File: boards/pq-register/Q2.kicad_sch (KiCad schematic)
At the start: 94 parts, among them Q100 MMBT5401, Q65 MMBT5401, Q73 MMBT5401, Q74 MMBT5401, Q75 MMBT5401, Q76 MMBT5401, Q77 MMBT5401, Q78 MMBT5401, Q79 MMBT5401, Q80 MMBT5401, Q81 MMBT5401, Q82 MMBT5401

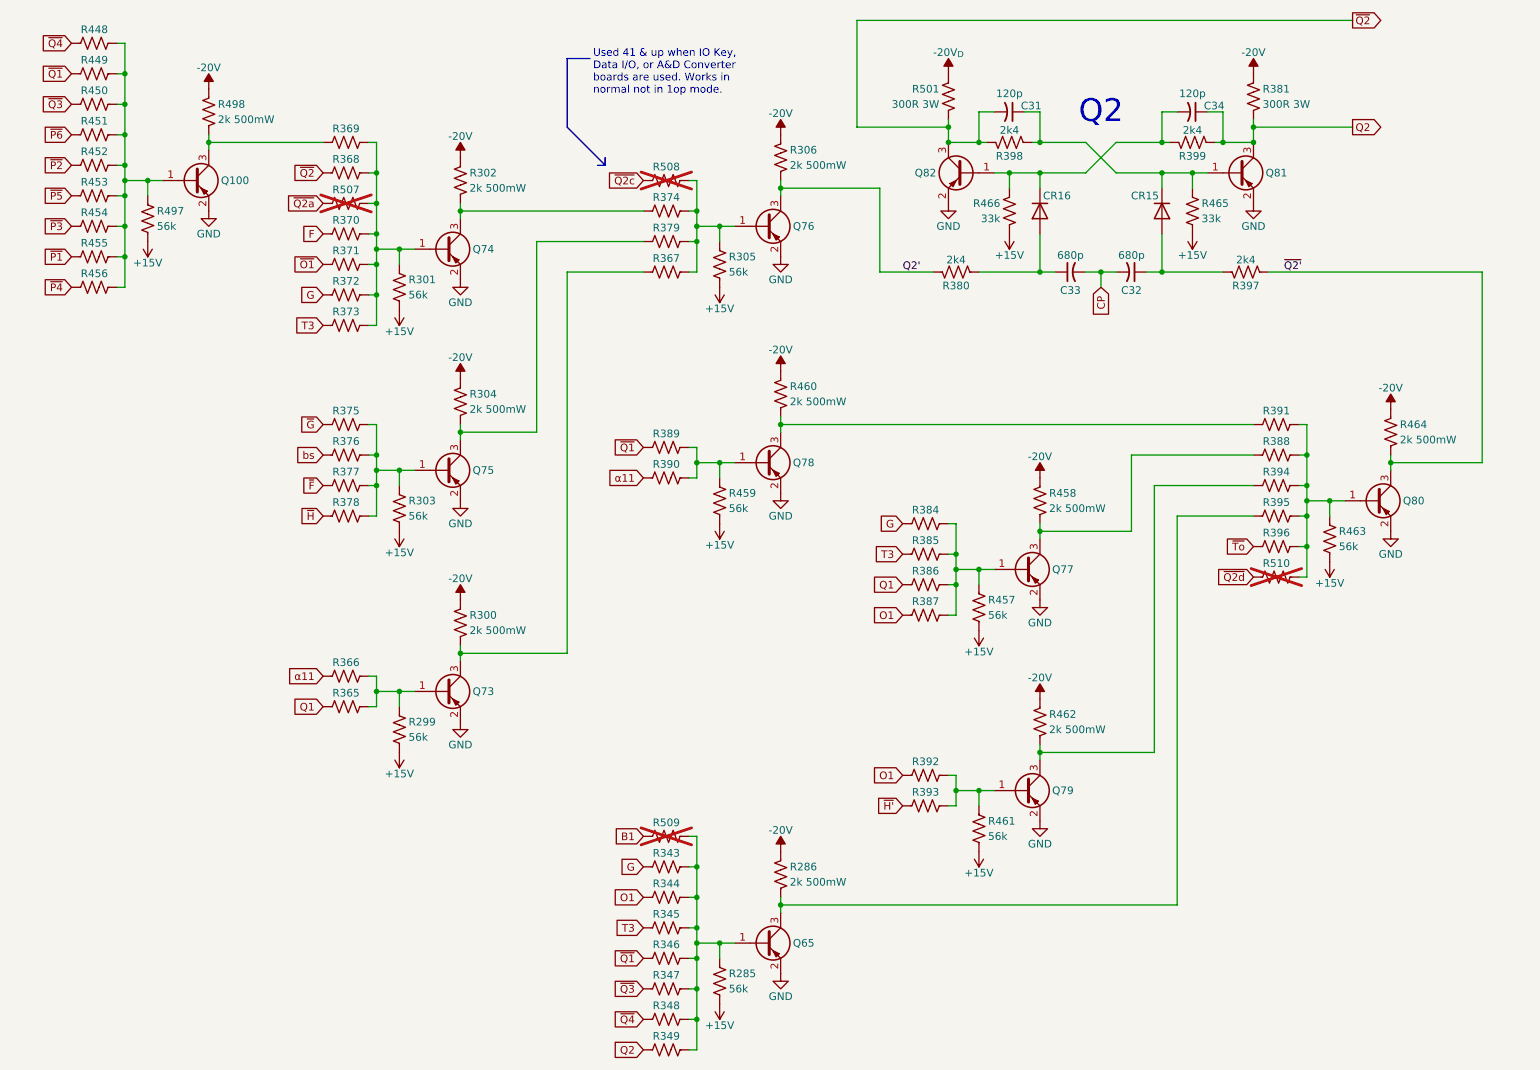
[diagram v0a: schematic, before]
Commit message: Better PCI footprint, more layout.
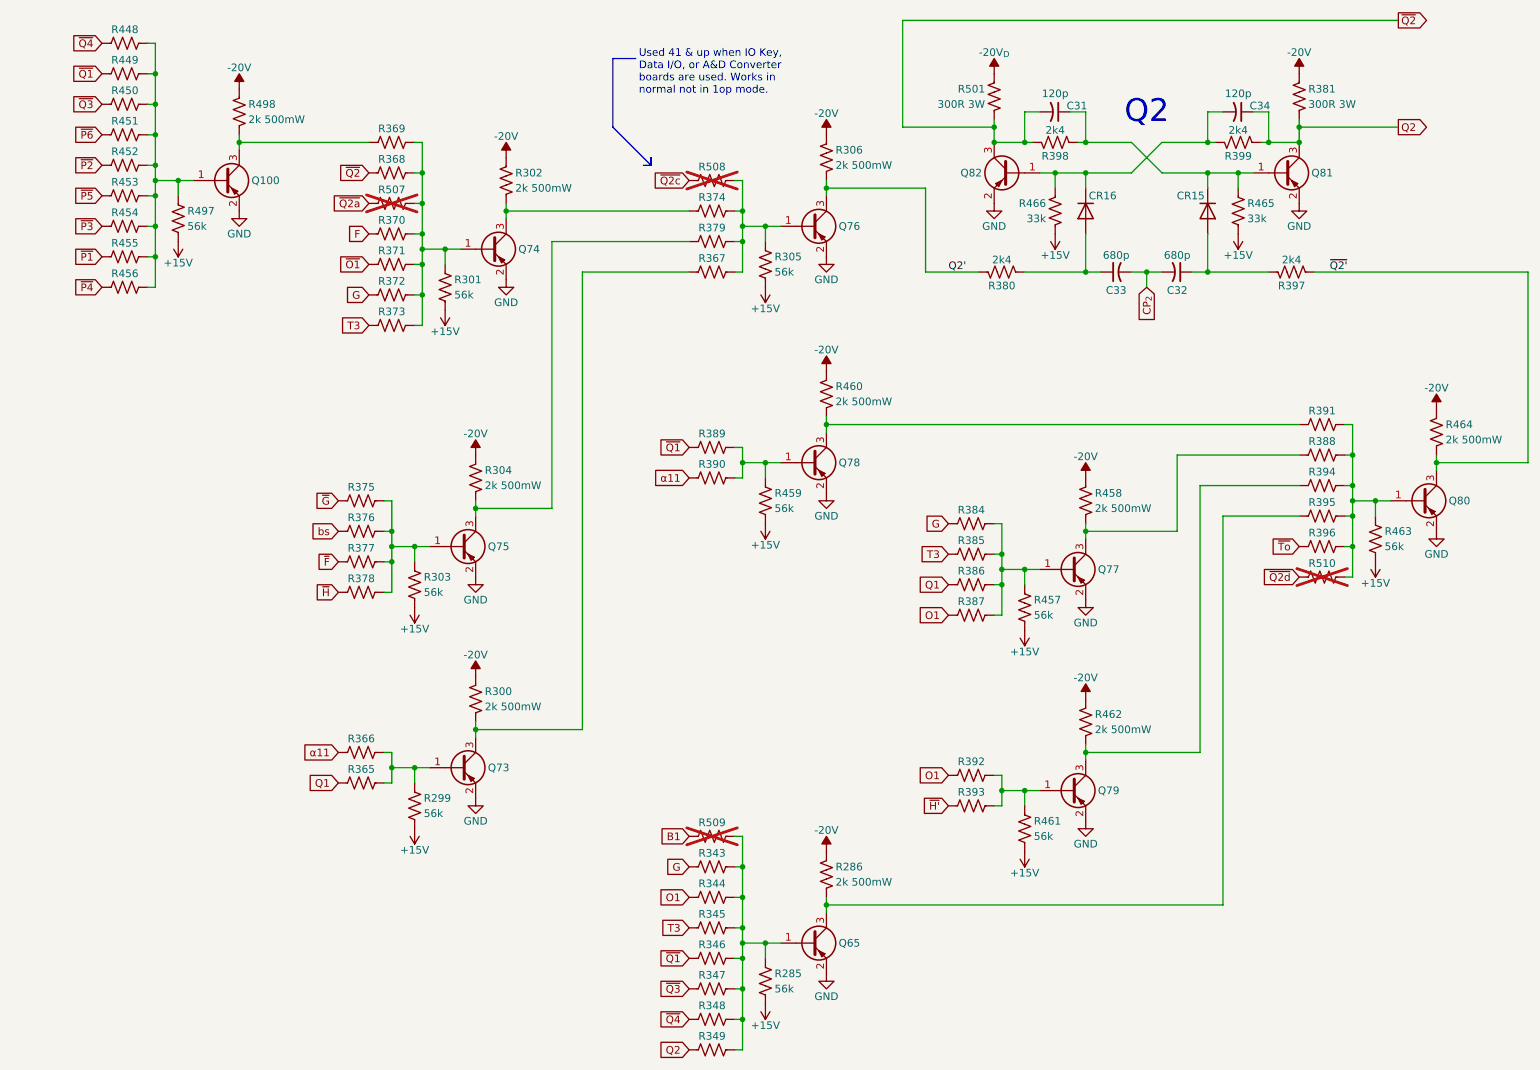
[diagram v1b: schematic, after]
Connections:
- net CP renamed CP_{2}
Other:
- moved on the sheet: C31, C32, C33, C34, CR15, CR16, Q100, Q65, Q73, Q74, Q75, Q76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

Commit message: Start updating 2k4 resistors to 0603, melt some traces.
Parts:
- R286, R300, R302, R304, R306, R458, R460, R462, R464, R498: value 2k 500mW -> 2k ½W
- R380, R397, R398, R399: value 2k4 -> 2k4 ¼W; footprint Resistor_SMD:R_0402_1005Metric -> Resistor_SMD:R_0603_1608Metric
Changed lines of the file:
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@@
 			)
 		)
-		(property "Value" "2k 500mW"
+		(property "Value" "2k ½W"
 			(at 90.424 135.89 0)
 			(show_name no)
@@
 			)
 		)
-		(property "Value" "2k 500mW"
+		(property "Value" "2k ½W"
 			(at 90.424 99.06 0)
 			(show_name no)
@@
 			)
 		)
-		(property "Value" "2k 500mW"
+		(property "Value" "2k ½W"
 			(at 250.444 91.44 0)
 			(show_name no)
@@
 			)
 		)
-		(property "Value" "2k4"
+		(property "Value" "2k4 ¼W"
 			(at 215.9 39.878 90)
 			(show_name no)
@@
 			)
 		)
-		(property "Footprint" "Resistor_SMD:R_0402_1005Metric"
+		(property "Footprint" "Resistor_SMD:R_0603_1608Metric"
 			(at 216.154 42.926 90)
 			(hide yes)
@@
 			)
 		)
-		(property "Value" "2k 500mW"
+		(property "Value" "2k ½W"
 			(at 192.024 102.87 0)
 			(show_name no)
@@
 			)
 		)
-		(property "Value" "2k 500mW"
+		(property "Value" "2k ½W"
 			(at 51.054 38.1 0)
 			(show_name no)
@@
 			)
 		)
-		(property "Value" "2k4"
+		(property "Value" "2k4 ¼W"
 			(at 176.53 61.468 90)
 			(show_name no)
@@
 			)
 		)
-		(property "Footprint" "Resistor_SMD:R_0402_1005Metric"
+		(property "Footprint" "Resistor_SMD:R_0603_1608Metric"
 			(at 176.784 64.516 90)
 			(hide yes)
@@
 			)
 		)
-		(property "Value" "2k 500mW"
+		(property "Value" "2k ½W"
 			(at 148.844 45.72 0)
 			(show_name no)
@@
 			)
 		)
-		(property "Value" "2k 500mW"
+		(property "Value" "2k ½W"
 			(at 95.504 49.53 0)
 			(show_name no)
@@
 			)
 		)
-		(property "Value" "2k4"
+		(property "Value" "2k4 ¼W"
 			(at 185.42 39.878 90)
 			(show_name no)
@@
 			)
 		)
-		(property "Footprint" "Resistor_SMD:R_0402_1005Metric"
+		(property "Footprint" "Resistor_SMD:R_0603_1608Metric"
 			(at 185.674 42.926 90)
 			(hide yes)
@@
 			)
 		)
-		(property "Value" "2k 500mW"
+		(property "Value" "2k ½W"
 			(at 148.844 85.09 0)
 			(show_name no)
@@
 			)
 		)
-		(property "Value" "2k 500mW"
+		(property "Value" "2k ½W"
 			(at 192.024 139.7 0)
 			(show_name no)
@@
 			)
 		)
-		(property "Value" "2k 500mW"
+		(property "Value" "2k ½W"
 			(at 148.844 165.1 0)
 			(show_name no)
@@
 			)
 		)
-		(property "Value" "2k4"
+		(property "Value" "2k4 ¼W"
 			(at 224.79 61.468 90)
 			(show_name no)
@@
 			)
 		)
-		(property "Footprint" "Resistor_SMD:R_0402_1005Metric"
+		(property "Footprint" "Resistor_SMD:R_0603_1608Metric"
 			(at 225.044 64.516 90)
 			(hide yes)

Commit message: Clean up sheet frames.
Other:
- company: © 1962 General Precision; redrawn by Sam Hanes -> © 2026 Sam Hanes, licensed CERN-OHL-W v2
- title: LGP-21 P & Q Register Board -> LGP-21 Mini - P&Q Register
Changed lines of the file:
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@@
 	(generator "eeschema")
 	(generator_version "10.0")
-	(paper "A")
+	(paper "USLetter")
 	(title_block
-		(title "LGP-21 P & Q Register Board")
-		(date "2026-06-15")
-		(rev "ESD 1060")
-		(company "© 1962 General Precision; redrawn by Sam Hanes")
-		(comment 1 "https://github.com/Elemecca/lgp21-docs")
+		(title "LGP-21 Mini - P&Q Register")
+		(date "2026-06-28")
+		(rev "A")
+		(company "© 2026 Sam Hanes, licensed CERN-OHL-W v2")
+		(comment 1 "https://github.com/Elemecca/lgp21-mini")
 	)
 	(text "Used 41 & up when IO Key,\nData I/O, or A&D Converter\nboards are used. Works in\nnormal not in 1op mode."
